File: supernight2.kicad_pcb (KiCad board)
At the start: 4 copper layers, 89.7 x 56.4 mm, 71 parts, among them J1 POWER IN, J3 Programming Header, J4 Debug Header, J5 POWER OUT, Q1 BC847C, Q2 CH1_MOS, Q3 CH2_MOS, SW1 SW_SPST, SW2 Rotary_Encoder_Switch, SW3 Rotary_Encoder_Switch, U1 ESP32, U2 LMR33640ADDA, U3 LMR33610ADDA, U4 EL7202CN

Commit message: first layout pass finished
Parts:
- removed J3: Programming Header, Connector_PinHeader_1.27mm:PinHeader_2x03_P1.27mm_Vertical
- removed J4: Debug Header, Connector_PinHeader_1.27mm:PinHeader_2x03_P1.27mm_Vertical
- removed SW2, SW3: Rotary_Encoder_Switch, Rotary_Encoder:RotaryEncoder_Alps_EC11E-Switch_Vertical_H20mm
- added J2: Conn_02x04_Odd_Even, Connector_JST:JST_SH_BM08B-SRSS-TB_1x08-1MP_P1.00mm_Vertical, F.Cu at (166.9, 80.9)
- added JTAG1: Prog Header, Connector_Samtec_HLE_THT:Samtec_HLE-105-02-xx-DV-TE_2x05_P2.54mm_Horizontal, F.Cu at (154.8, 85.1)
- 12V_SW1, 12v_PWGD1, 3V3_PWGD1, 3V3_SW1, ESP_TX1, TP1, TP6, TP7, TP8, TP9: moved to B.Cu
- moved TP6 213.9 mm to (151.5, 114.9)
- moved C23 206.2 mm to (150.6, 112.0)
- moved R18 177.6 mm to (168.5, 95.5), turned to 180 degrees
- moved TP9 173.4 mm to (144.5, 105.2)
- moved R4 168.3 mm to (146.4, 111.1), turned to 270 degrees
- moved TP7 166.8 mm to (153.5, 108.3)
- moved TP8 158.8 mm to (164.8, 99.1)
- moved J5 93.6 mm to (187.2, 109.2), turned to 270 degrees
- moved TH1 84.1 mm to (164.1, 95.9), turned to 180 degrees
- moved R8 84.1 mm to (173.1, 84.1), turned to 270 degrees
- moved J1 83.2 mm to (113.5, 92.5)
- moved C14 81.1 mm to (118.0, 117.1)
- moved C21 81.1 mm to (136.5, 110.0)
- moved C22 81.1 mm to (132.0, 110.0)
- moved 12V_SW1 81.1 mm to (121.5, 100.3)
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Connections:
- R8 pad 1: /ESP_EN_R -> +3V3
- R8 pad 2: ESP_EN -> ESP_SLP_L
- SW1 pad 1: ESP_EN -> ESP_SLP_L
- U1 pad 12: Net-(U1-Pad12) -> ESP_SLP_L
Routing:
- net +3V3: track 62.7 -> 152.9 mm, vias 7 -> 10
- net 12v_EN: track 7.77 -> 84.6 mm
- net /ESP_EN_R: track 56.3 -> 0.00 mm, vias 1 -> 0
- net Net-(R4-Pad2): track 0.00 -> 55.6 mm, vias 0 -> 2
- net ESP_SLP_L: track 0.00 -> 54.1 mm, vias 0 -> 2
- net Net-(R3-Pad2): track 0.00 -> 46.8 mm, vias 0 -> 2
- net ESP_BOOT_L: track 0.00 -> 41.8 mm, vias 0 -> 1
- net TDO: track 0.00 -> 41.2 mm
- net TEMP_FB: track 0.00 -> 37.7 mm, vias 0 -> 2
- net TMS: track 0.00 -> 32.1 mm
- net ESP_TXD: track 0.00 -> 31.4 mm, vias 0 -> 2
- net TCK: track 0.00 -> 29.7 mm
- net ROT2_A: track 0.00 -> 28.6 mm, vias 0 -> 2
- net ROT2_B: track 0.00 -> 27.8 mm, vias 0 -> 2
- net BTN_SEL_2: track 0.00 -> 27.4 mm, vias 0 -> 2
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- added copper zone on B.Cu, net Net-(J5-Pad3)
- added copper zone on B.Cu, net Net-(J5-Pad4)

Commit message: soft release v0.2
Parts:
- removed OLED1: OLED Connector, Connector_JST:JST_SH_SM04B-SRSS-TB_1x04-1MP_P1.00mm_Horizontal
- added OLED: OLED Connector, Connector_JST:JST_SH_BM04B-SRSS-TB_1x04-1MP_P1.00mm_Vertical, F.Cu at (199.8, 84.8)
- added REF**: MountingHole_3.2mm_M3_ISO14580_Pad_TopBottom, MountingHole:MountingHole_3.2mm_M3_ISO14580_Pad_TopBottom, F.Cu at (199.0, 115.5)
- added REF**: MountingHole_3.2mm_M3_ISO14580_Pad_TopBottom, MountingHole:MountingHole_3.2mm_M3_ISO14580_Pad_TopBottom, F.Cu at (199.0, 73.6)
- added REF**: MountingHole_3.2mm_M3_ISO14580_Pad_TopBottom, MountingHole:MountingHole_3.2mm_M3_ISO14580_Pad_TopBottom, F.Cu at (119.8, 115.5)
- added REF**: MountingHole_3.2mm_M3_ISO14580_Pad_TopBottom, MountingHole:MountingHole_3.2mm_M3_ISO14580_Pad_TopBottom, F.Cu at (119.8, 67.2)
- added REF**: R_0612_1632Metric_Pad1.18x3.40mm_HandSolder, Resistor_SMD:R_0612_1632Metric_Pad1.18x3.40mm_HandSolder, F.Cu at (180.1, 113.5)
- added REF**: R_0612_1632Metric_Pad1.18x3.40mm_HandSolder, Resistor_SMD:R_0612_1632Metric_Pad1.18x3.40mm_HandSolder, F.Cu at (176.1, 100.6)
- C10, C11: footprint Capacitor_SMD:C_0805_2012Metric -> Capacitor_SMD:C_1206_3216Metric
- J1: value POWER IN -> 43045-0421
- J5: value POWER OUT -> 43045-0421
- JTAG: renamed from JTAG1; value Prog Header -> HTST-105-01-T-DV
- L2: footprint Inductor_SMD:L_Bourns_SRR1260 -> Inductor_SMD:L_Bourns_PM42S
- Q2: value CH1_MOS -> DMN3010LK3
- Q3: value CH2_MOS -> DMN3010LK3
- moved J2 38.0 mm to (199.8, 99.8), turned to 270 degrees
- moved C19 27.8 mm to (135.5, 75.2), turned to 0 degrees
- moved 3V3_SW1 20.4 mm to (136.8, 68.5)
- moved C18 19.1 mm to (130.5, 73.8)
- moved C6 18.4 mm to (147.0, 78.2), turned to 0 degrees
- moved C20 17.5 mm to (151.8, 104.8)
- moved L2 17.3 mm to (136.8, 70.0), turned to 270 degrees
- moved C11 17.2 mm to (145.7, 80.5), turned to 0 degrees
- moved C2 16.8 mm to (136.0, 83.6), turned to 180 degrees
- moved C22 15.3 mm to (147.2, 110.4)
- moved C9 14.9 mm to (132.3, 106.8)
- moved R11 14.9 mm to (126.5, 114.7)
- moved R9 14.9 mm to (126.5, 113.2)
- moved U2 14.9 mm to (130.8, 111.6)
- moved 12V_SW1 14.9 mm to (136.4, 100.7)
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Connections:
- net CH1_SIG renamed CH1_SIG_R
- net CH2_SIG renamed CH2_SIG_R
- net Net-(J5-Pad3) renamed /MOSFET_DRIVE/LED_L_1
- net Net-(J5-Pad4) renamed /MOSFET_DRIVE/LED_L_2
- net Net-(R3-Pad2) renamed /CH1_SIG
- net Net-(R4-Pad2) renamed /CH2_SIG
- Q1 pad 1: ESP_TXD -> ESP_TX
- U1 pad 34: ESP_RXD -> ESP_RX
- U1 pad 35: ESP_TXD -> ESP_TX
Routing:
- net 12v_PWGD: track 0.00 -> 110.5 mm, vias 0 -> 4
- net +3V3: track 152.9 -> 94.4 mm, vias 10 -> 11
- net ESP_TX: track 0.00 -> 55.9 mm, vias 0 -> 3
- net ESP_RX: track 0.00 -> 51.3 mm, vias 0 -> 1
- net ROT1_B: track 7.86 -> 39.6 mm, vias 0 -> 2
- net ESP_TXD: track 31.4 -> 0.00 mm, vias 2 -> 0
- net ROT1_A: track 8.46 -> 36.9 mm, vias 0 -> 2
- net BTN_SEL_1: track 16.7 -> 41.4 mm, vias 0 -> 2
- net /TX LED/ESP_TX_BUFF: track 2.26 -> 22.9 mm, vias 0 -> 2
- net /VDD_SENSE_R: track 0.00 -> 20.1 mm, vias 0 -> 2
- net 12v_EN: track 84.6 -> 64.6 mm, vias 2 -> 4
- net GND: track 5.73 -> 21.8 mm, vias 1 -> 67
- net ESP_EN: track 64.5 -> 48.4 mm
- net /VDD_SENSE: track 34.8 -> 21.7 mm, vias 2 -> 0
- net /Power Supply/12V_SW: track 2.34 -> 11.4 mm, vias 0 -> 1
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- added copper zone on In2.Cu, net +12V
- added copper zone on F.Cu, net /MOSFET_DRIVE/LED_L_1
- added copper zone on F.Cu, net /MOSFET_DRIVE/LED_L_2
- added copper zone on B.Cu, net GND
- removed copper zone on B.Cu, net +12V
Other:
- board size 89.7 x 56.4 mm -> 87.2 x 56.2 mm
- rule via_min_size: 0.4 -> 0.3

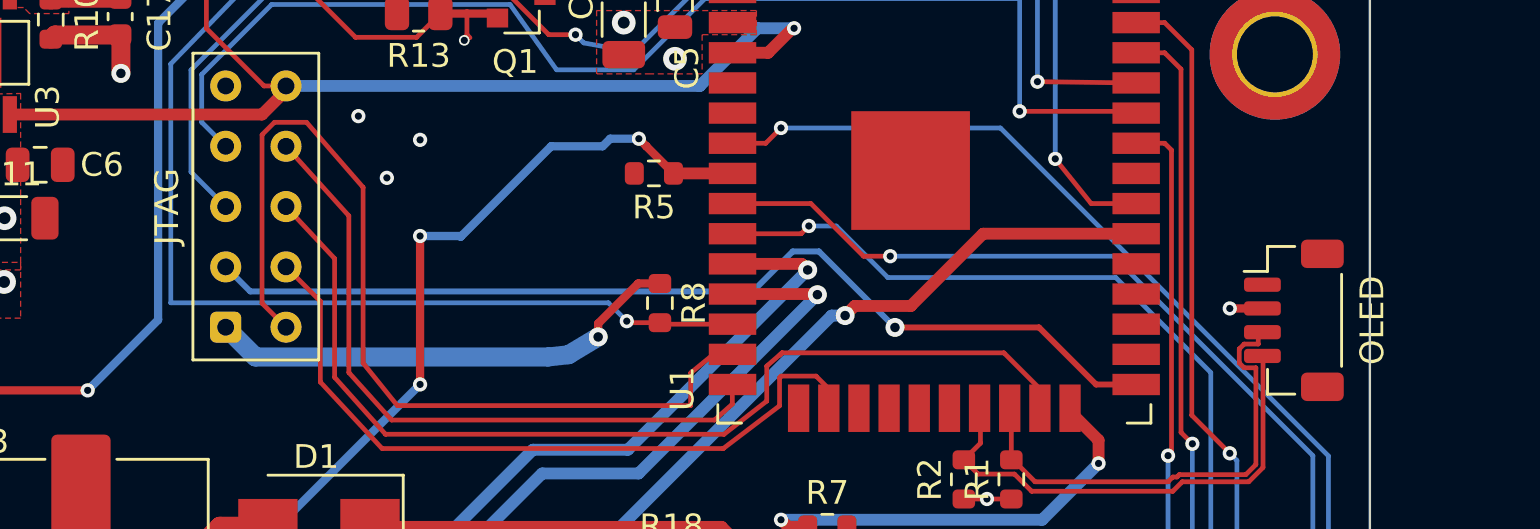
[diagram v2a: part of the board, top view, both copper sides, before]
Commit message: changed connector locations
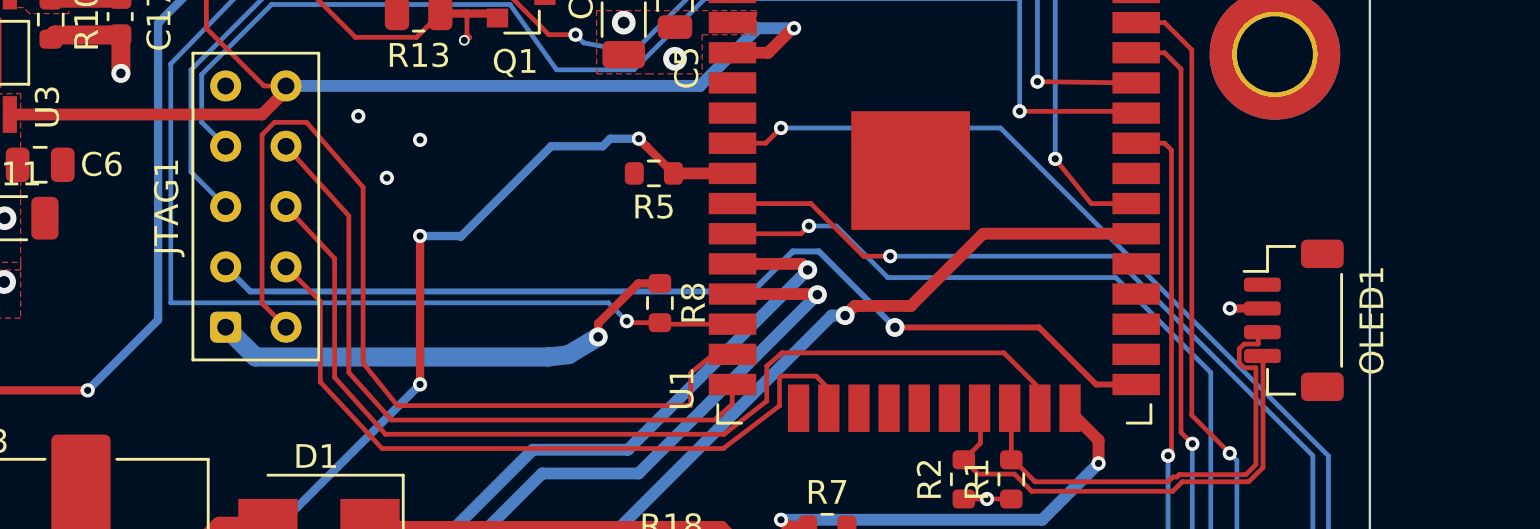
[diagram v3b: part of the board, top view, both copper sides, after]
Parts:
- Q2, Q3: value DMN3010LK3 -> FDD8451
- renumbered JTAG to JTAG1, OLED to OLED1
